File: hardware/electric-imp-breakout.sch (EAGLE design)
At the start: 22 parts, among them Q1 DMG2307L-7, U1 ELECTRIC_IMP, U2 TPS62172, U3 ATSHA204-TSU, X1 USBSMD

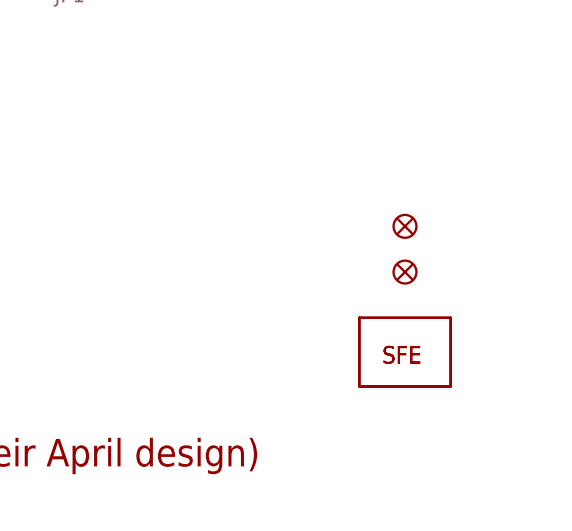
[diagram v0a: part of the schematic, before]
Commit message: changed micro fid to regular
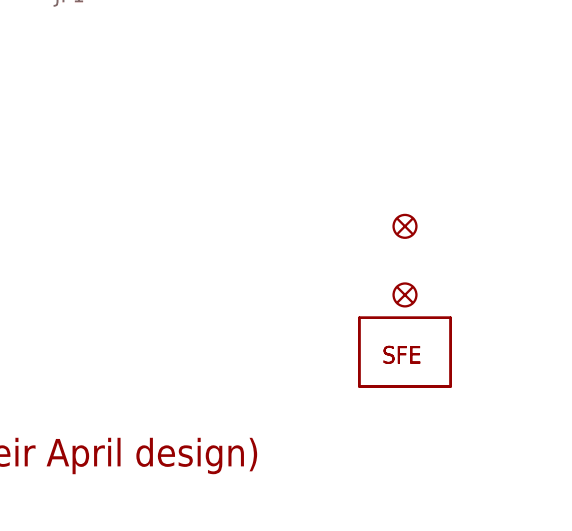
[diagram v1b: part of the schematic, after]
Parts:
- removed JP8, JP9: FIDUCIALUFIDUCIAL, SparkFun:FIDUCIALUFIDUCIAL
- added FID1, FID2: FIDUCIAL1X2, SparkFun-Aesthetics:FIDUCIAL1X2
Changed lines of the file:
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@@
 <?xml version="1.0" encoding="utf-8"?>
 <!DOCTYPE eagle SYSTEM "eagle.dtd">
-<eagle version="6.5.0">
+<eagle version="6.6.0">
 <drawing>
 <settings>
@@
 <layer number="106" name="bPlate" color="7" fill="1" visible="no" active="yes"/>
 <layer number="107" name="Crop" color="7" fill="1" visible="no" active="yes"/>
+<layer number="108" name="tplace-old" color="10" fill="1" visible="no" active="yes"/>
+<layer number="109" name="ref-old" color="11" fill="1" visible="no" active="yes"/>
 <layer number="116" name="Patch_BOT" color="9" fill="4" visible="no" active="yes"/>
 <layer number="121" name="_tsilk" color="7" fill="1" visible="no" active="yes"/>
@@
 <layer number="144" name="Drill_legend" color="7" fill="1" visible="no" active="yes"/>
 <layer number="151" name="HeatSink" color="7" fill="1" visible="no" active="yes"/>
+<layer number="199" name="Contour" color="7" fill="1" visible="yes" active="yes"/>
 <layer number="200" name="200bmp" color="1" fill="10" visible="no" active="yes"/>
 <layer number="201" name="201bmp" color="2" fill="10" visible="no" active="yes"/>
@@
 <part name="JP7" library="SparkFun-Aesthetics" deviceset="LOGO-SFE" device="NEW"/>
 <part name="U$5" library="SparkFun-Aesthetics" deviceset="OSHW-LOGO" device="S"/>
-<part name="JP8" library="SparkFun" deviceset="FIDUCIAL" device="UFIDUCIAL"/>
-<part name="JP9" library="SparkFun" deviceset="FIDUCIAL" device="UFIDUCIAL"/>
+<part name="FID1" library="SparkFun-Aesthetics" deviceset="FIDUCIAL" device="1X2"/>
+<part name="FID2" library="SparkFun-Aesthetics" deviceset="FIDUCIAL" device="1X2"/>
 </parts>
 <sheets>
@@
 <instance part="JP7" gate="G$1" x="241.3" y="17.78"/>
 <instance part="U$5" gate="G$1" x="132.08" y="10.16"/>
-<instance part="JP8" gate="G$1" x="243.84" y="33.02"/>
-<instance part="JP9" gate="G$1" x="243.84" y="27.94"/>
+<instance part="FID1" gate="G$1" x="243.84" y="33.02"/>
+<instance part="FID2" gate="G$1" x="243.84" y="25.4"/>
 </instances>
 <busses>
